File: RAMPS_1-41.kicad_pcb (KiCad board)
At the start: 2 copper layers, 101.6 x 60.3 mm, 85 parts, among them J1 282837-6, J2 Conn_01x02, J3 Conn_01x03, J4 Conn_01x06, J5 Conn_01x04, Q1 STP55NF06L, Q2 STP55NF06L, Q3 STP55NF06L, U1 ARDUINO_MEGA_SHIELD, U2 A4988BREAKOUT, U3 A4988BREAKOUT, U4 A4988BREAKOUT, U5 A4988BREAKOUT, U6 A4988BREAKOUT, X4 MSTBA4

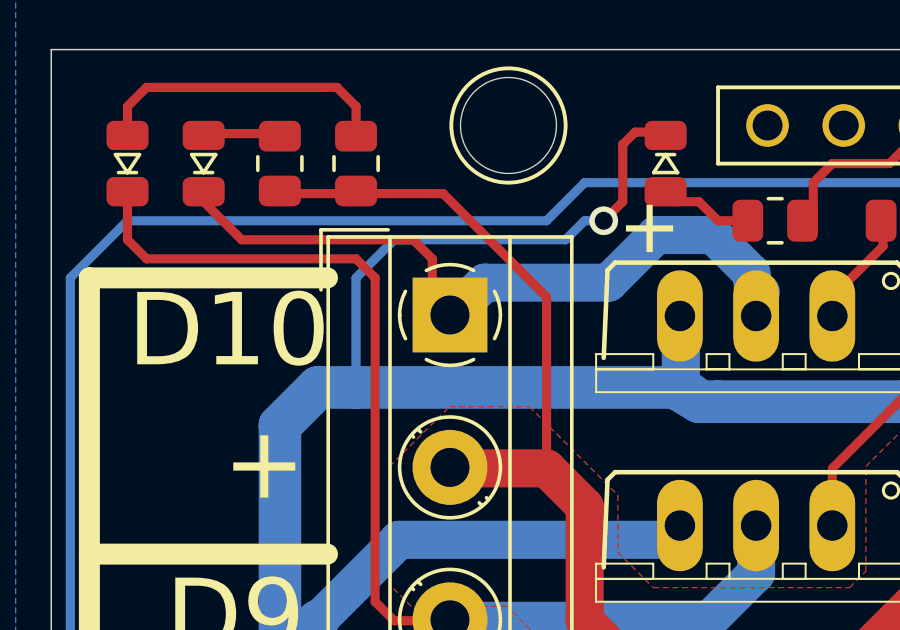
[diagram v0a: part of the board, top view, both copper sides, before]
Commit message: Kicad 8 updates
Remove unused files
Update schematic and PCB files to Kicad 8 format
"Rescue" some symbols
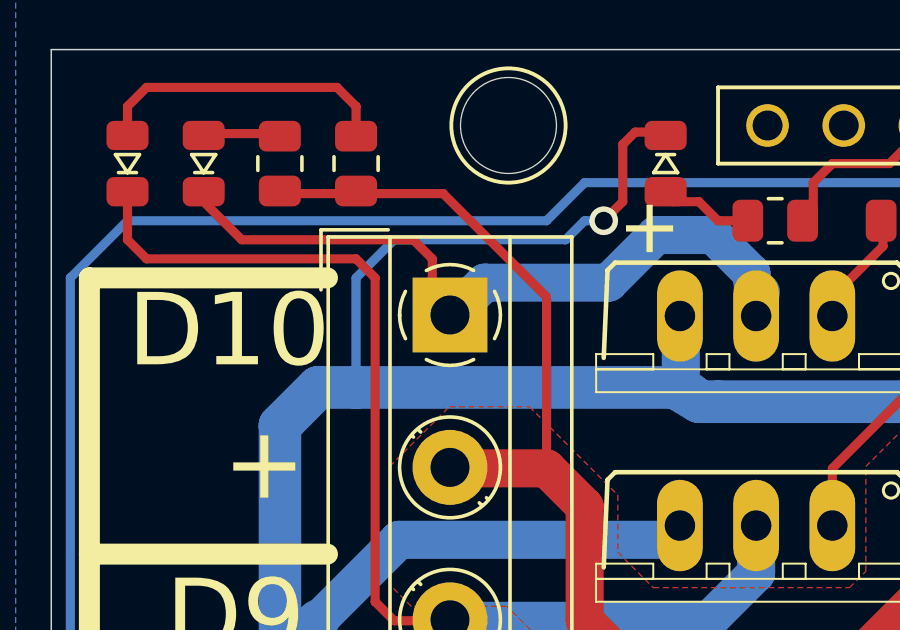
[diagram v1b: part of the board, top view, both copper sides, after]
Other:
- net class Default removed

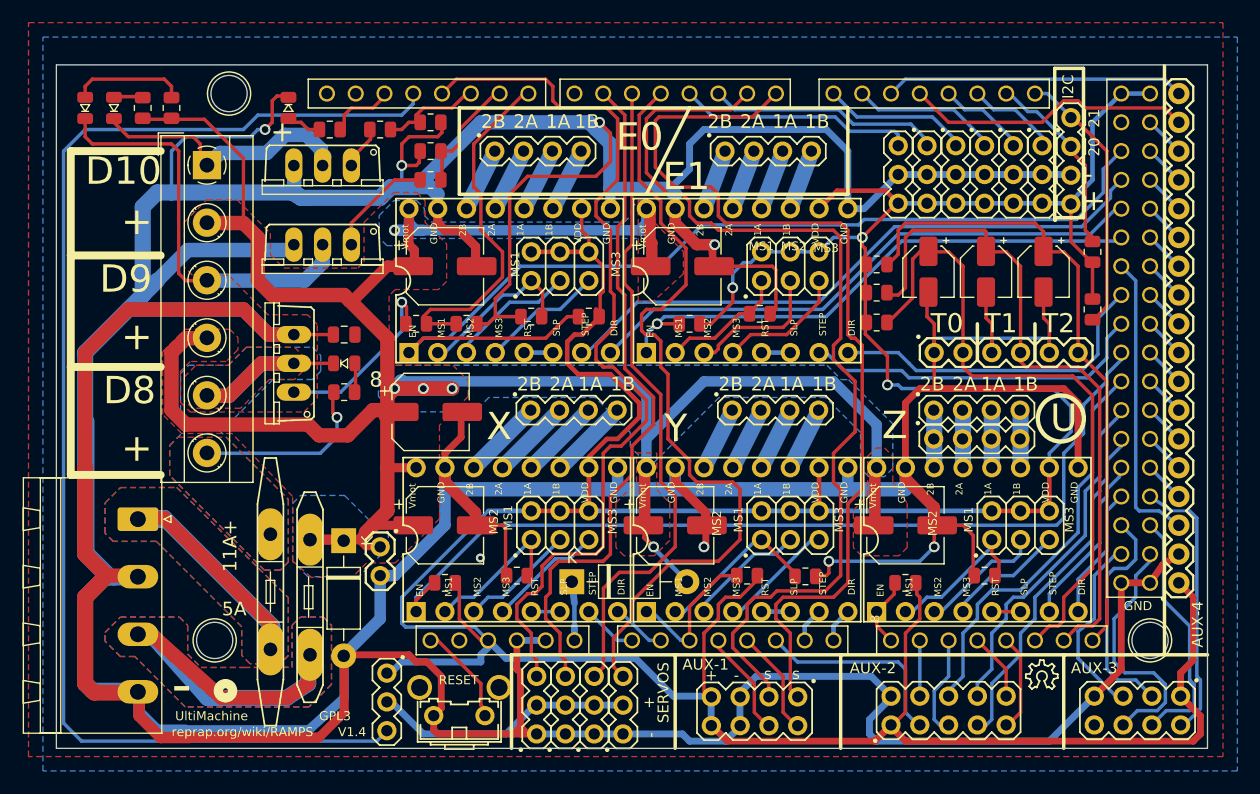
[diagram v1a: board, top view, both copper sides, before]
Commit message: Cleanup of imported PCB
Fix traces with insufficient clearance
Removed unused markings from User.Drawings and User.Eco1
Tidy up silkscreen and add a few additional markings
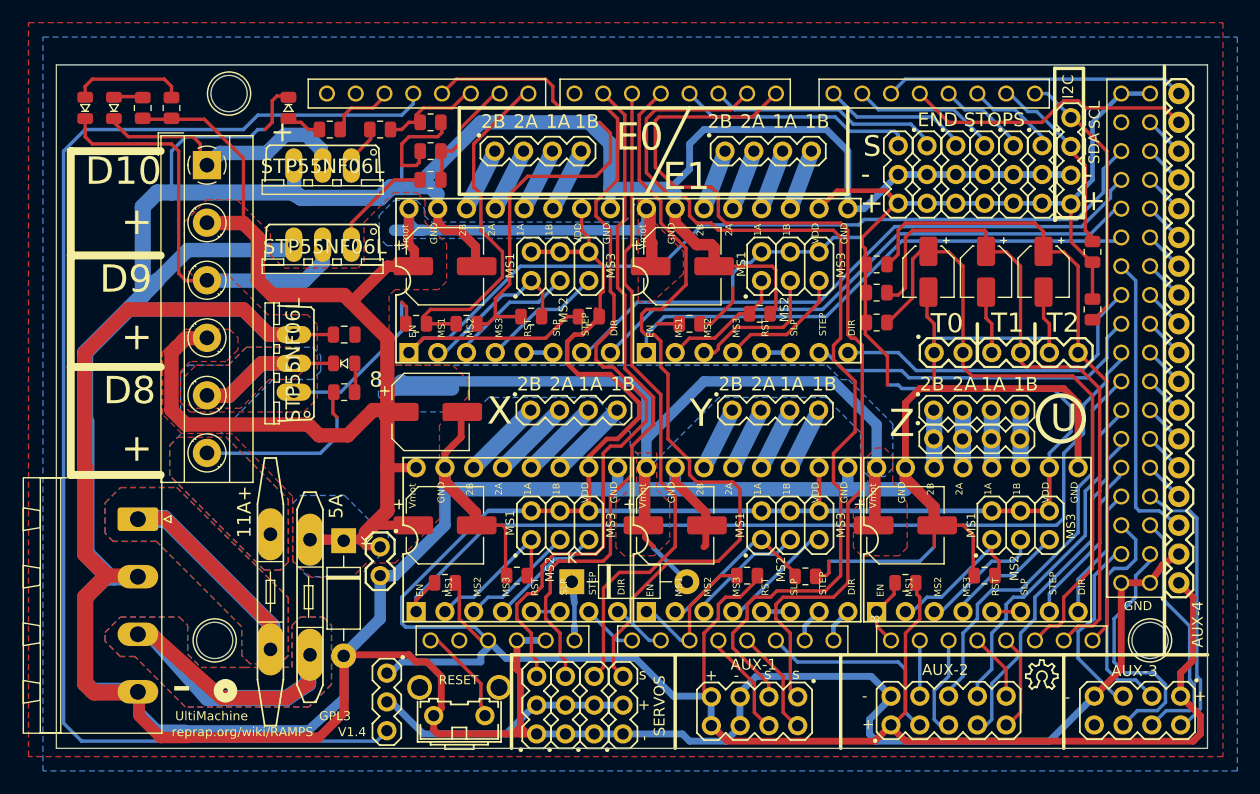
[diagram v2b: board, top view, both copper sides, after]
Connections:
- AUX3 pad 8: (no net) -> unconnected-(AUX3-Pin_8-Pad8)
- U1 pad 3.3V: (no net) -> unconnected-(U1-Pad3.3V)
- U1 pad AREF: (no net) -> unconnected-(U1-PadAREF)
- U1 pad D22: (no net) -> unconnected-(U1-PadD22)
- U1 pad D7: (no net) -> unconnected-(U1-PadD7)
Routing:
- net +12V: track 229.8 -> 223.8 mm, vias 5 -> 0
- net GND: track 715.0 -> 713.6 mm, vias 8 -> 0
- net VCC: vias 3 -> 0
- net Net-(Q3-G): vias 1 -> 0
- net /E1-EN: vias 1 -> 0
- net +12P: vias 1 -> 0
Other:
- board text added: "SCL"
- board text added: "SDA"
- board text removed: "1"
- board text removed: "FillOverPAD:+12V2:146:414"
- board text removed: "FillOverPAD:+12V:10:414"
- board text removed: "FillOverPAD:+12V:12:414"
- board text removed: "FillOverPAD:+12V:148:414"
- board text removed: "FillOverPAD:+12V:14:414"
- board text removed: "FillOverPAD:+12V:150:414"
- board text removed: "FillOverPAD:+12V:18:414"
- board text removed: "FillOverPAD:+12V:20:414"
- board text removed: "FillOverPAD:+12V:24:414"
- board text removed: "FillOverPAD:+12V:26:414"
- board text removed: "FillOverPAD:GND:105:414"
- board text removed: "FillOverPAD:GND:107:414"
- board text removed: "FillOverPAD:GND:109:414"
- board text removed: "FillOverPAD:GND:111:414"
- board text removed: "FillOverPAD:GND:112:414"
- board text removed: "FillOverPAD:GND:117:414"
- board text removed: "FillOverPAD:GND:119:414"
- board text removed: "FillOverPAD:GND:11:414"
- board text removed: "FillOverPAD:GND:121:414"
- board text removed: "FillOverPAD:GND:13:414"
- board text removed: "FillOverPAD:GND:15:414"
- board text removed: "FillOverPAD:GND:17:414"
- board text removed: "FillOverPAD:GND:19:414"
- board text removed: "FillOverPAD:GND:21:414"
- board text removed: "FillOverPAD:GND:23:414"
- board text removed: "FillOverPAD:GND:25:414"
- board text removed: "FillOverPAD:GND:27:414"
- board text removed: "FillOverPAD:GND:85:414"
- board text removed: "FillOverPAD:GND:9:414"
- board text removed: "FillOverPAD:N$51:87:414"
- board text removed: "PS"
- board text removed: "TE:N$54:1:5::L16"
- board text removed: "TE:N$54:2:5::L16"
- board text removed: "TE:N$54:3:5::L16"
- board text removed: "TE:N$54:4:5::L16"
- board text removed: "TE:N$54:5:5::L16"
- board text removed: "TS:N$54:1:5::L16"
- board text removed: "TS:N$54:2:5::L16"
- board text removed: "TS:N$54:3:5::L16"
- board text removed: "TS:N$54:4:5::L16"
- board text removed: "TS:N$54:5:5::L16"
